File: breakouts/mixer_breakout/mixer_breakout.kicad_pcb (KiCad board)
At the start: 4 copper layers, 24 x 28.5 mm, 131 parts, among them P1 CONN_01X04, U101 CONN_SMA_2GND, U102 CONN_SMA_2GND, U103 CONN_SMA_2GND, U2 LTC5549

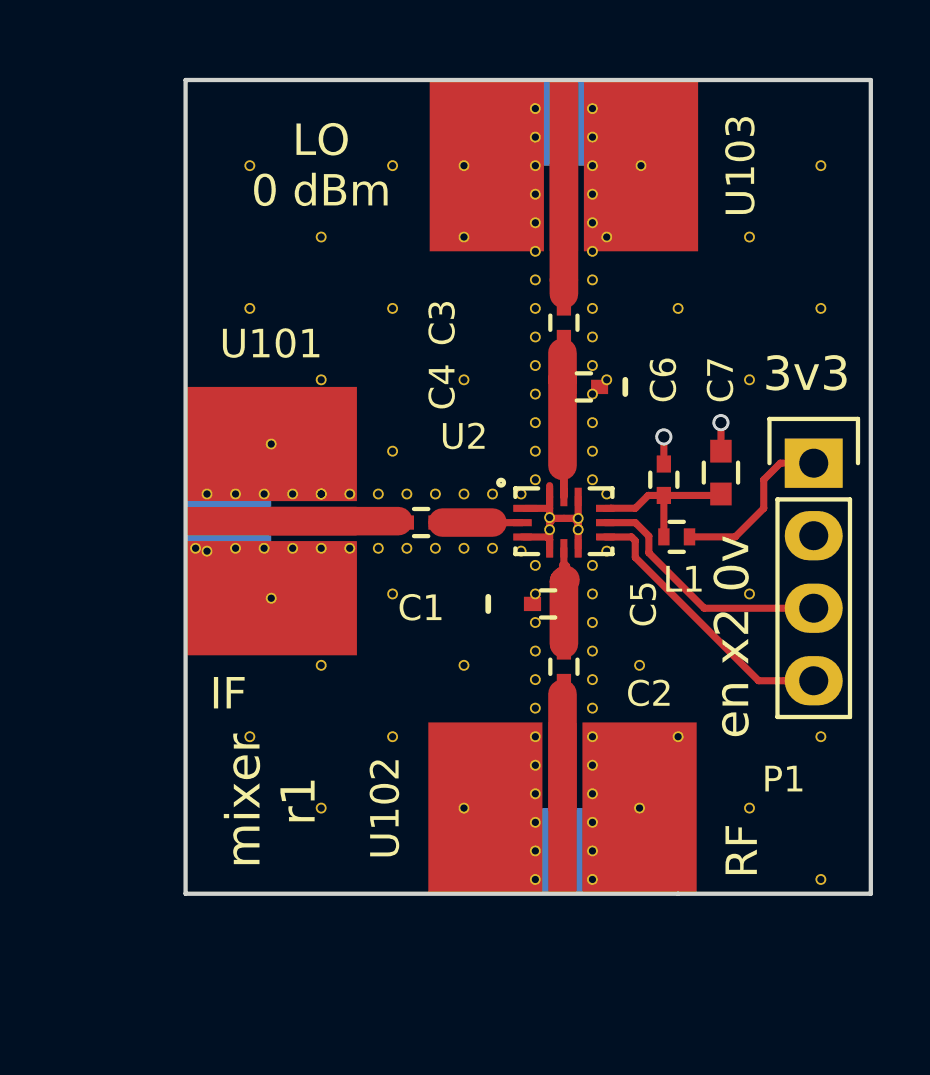
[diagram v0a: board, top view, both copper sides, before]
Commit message: modified mixer breakout to work with ltc5548, moved to soldermask defined pads
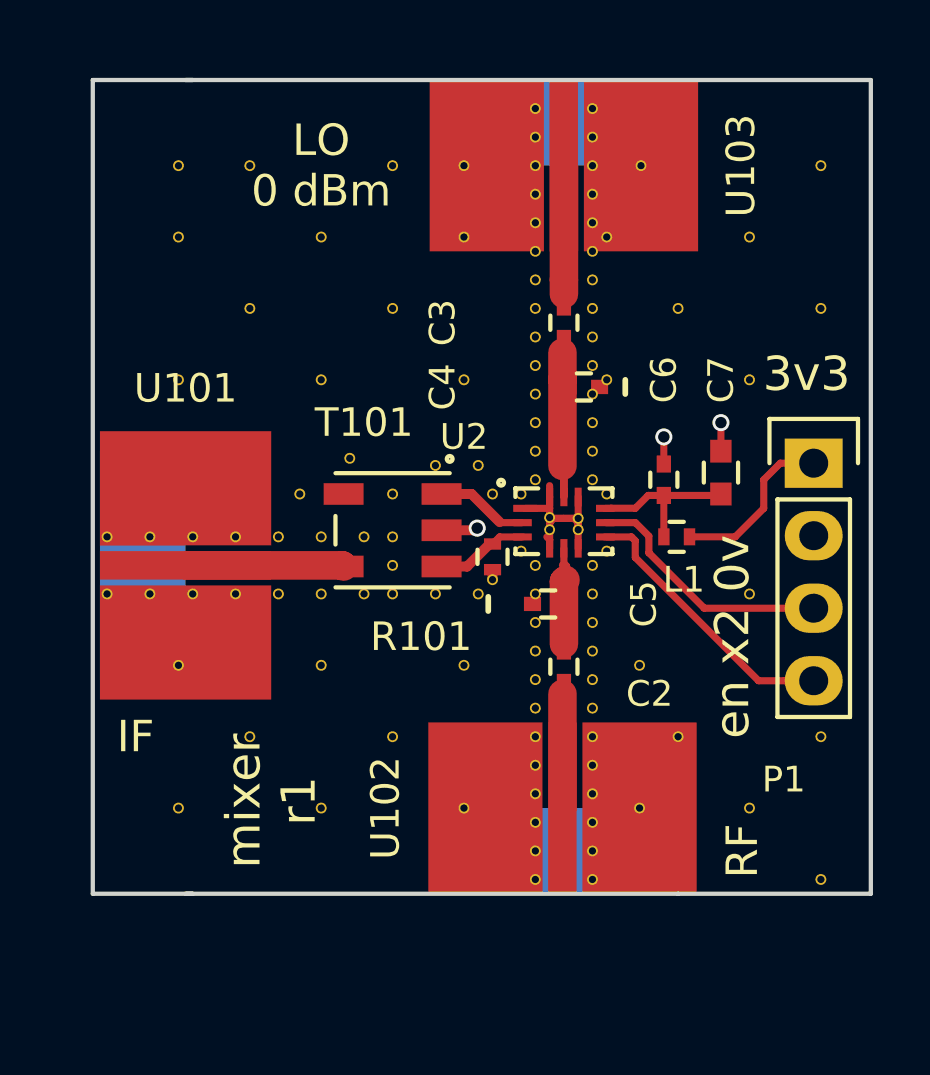
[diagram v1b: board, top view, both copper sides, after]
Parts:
- removed C1: 10 pF, Capacitors_SMD:C_0402
- removed the REF** at (138.2, 107.7)
- removed the REF** at (142.5, 102.5)
- removed the REF** at (142.0, 104.0)
- removed the REF** at (144.0, 104.0)
- removed the REF** at (143.0, 104.0)
- removed the REF** at (145.0, 104.0)
- removed the REF** at (145.0, 105.9)
- removed the REF** at (144.0, 105.9)
- removed the REF** at (143.0, 105.9)
- removed the REF** at (142.0, 105.9)
- removed the REF** at (141.0, 105.9)
- removed the REF** at (140.0, 105.9)
- removed the REF** at (139.0, 105.9)
- removed the REF** at (138.0, 105.9)
- removed the REF** at (137.0, 105.9)
- removed the REF** at (135.6, 105.9)
- removed the REF** at (138.2, 102.2)
- removed the REF** at (136.0, 106.0)
- removed the REF** at (136.0, 104.0)
- removed the REF** at (137.0, 104.0)
- removed the REF** at (138.0, 104.0)
- removed the REF** at (139.0, 104.0)
- added R101: R_Small, Resistors_SMD:R_0402, F.Cu at (146.0, 106.2)
- added REF**: VIA_OSH4LAYER_MIN, vna_footprints:VIA_OSH4LAYER_MIN, F.Cu at (135.0, 92.5)
- added REF**: VIA_OSH4LAYER_MIN, vna_footprints:VIA_OSH4LAYER_MIN, F.Cu at (135.0, 100.0)
- added REF**: VIA_OSH4LAYER_MIN, vna_footprints:VIA_OSH4LAYER_MIN, F.Cu at (135.0, 110.0)
- added REF**: VIA_OSH4LAYER_MIN, vna_footprints:VIA_OSH4LAYER_MIN, F.Cu at (135.0, 115.0)
- added REF**: VIA_OSH4LAYER_MIN, vna_footprints:VIA_OSH4LAYER_MIN, F.Cu at (137.0, 105.5)
- added REF**: VIA_OSH4LAYER_MIN, vna_footprints:VIA_OSH4LAYER_MIN, F.Cu at (134.0, 105.5)
- added REF**: VIA_OSH4LAYER_MIN, vna_footprints:VIA_OSH4LAYER_MIN, F.Cu at (135.5, 105.5)
- added REF**: VIA_OSH4LAYER_MIN, vna_footprints:VIA_OSH4LAYER_MIN, F.Cu at (138.5, 105.5)
- added REF**: VIA_OSH4LAYER_MIN, vna_footprints:VIA_OSH4LAYER_MIN, F.Cu at (140.0, 105.5)
- added REF**: VIA_OSH4LAYER_MIN, vna_footprints:VIA_OSH4LAYER_MIN, F.Cu at (141.5, 105.5)
- added REF**: VIA_OSH4LAYER_MIN, vna_footprints:VIA_OSH4LAYER_MIN, F.Cu at (141.5, 107.5)
- added REF**: VIA_OSH4LAYER_MIN, vna_footprints:VIA_OSH4LAYER_MIN, F.Cu at (142.5, 106.5)
- added REF**: VIA_OSH4LAYER_MIN, vna_footprints:VIA_OSH4LAYER_MIN, F.Cu at (140.0, 107.5)
- added REF**: VIA_OSH4LAYER_MIN, vna_footprints:VIA_OSH4LAYER_MIN, F.Cu at (138.5, 107.5)
- added REF**: VIA_OSH4LAYER_MIN, vna_footprints:VIA_OSH4LAYER_MIN, F.Cu at (137.0, 107.5)
- added REF**: VIA_OSH4LAYER_MIN, vna_footprints:VIA_OSH4LAYER_MIN, F.Cu at (135.5, 107.5)
- added REF**: VIA_OSH4LAYER_MIN, vna_footprints:VIA_OSH4LAYER_MIN, F.Cu at (134.0, 107.5)
- added REF**: VIA_OSH4LAYER_MIN, vna_footprints:VIA_OSH4LAYER_MIN, F.Cu at (132.5, 105.5)
- added REF**: VIA_OSH4LAYER_MIN, vna_footprints:VIA_OSH4LAYER_MIN, F.Cu at (132.5, 107.5)
- added REF**: VIA_OSH4LAYER_MIN, vna_footprints:VIA_OSH4LAYER_MIN, F.Cu at (142.5, 105.5)
- added REF**: VIA_OSH4LAYER_MIN, vna_footprints:VIA_OSH4LAYER_MIN, F.Cu at (145.5, 107.5)
- added REF**: VIA_OSH4LAYER_MIN, vna_footprints:VIA_OSH4LAYER_MIN, F.Cu at (145.5, 103.0)
- added REF**: VIA_OSH4LAYER_MIN, vna_footprints:VIA_OSH4LAYER_MIN, F.Cu at (144.0, 103.0)
- added REF**: VIA_OSH4LAYER_MIN, vna_footprints:VIA_OSH4LAYER_MIN, F.Cu at (144.0, 107.5)
- added REF**: VIA_OSH4LAYER_MIN, vna_footprints:VIA_OSH4LAYER_MIN, F.Cu at (135.0, 95.0)
- added T101: MABAES0060, vna_footprints:5LEAD_BALUN_4p83mm_3p3mm, F.Cu at (142.5, 105.3)
- moved U101 3.38 mm to (135.2, 106.5)
- moved REF** 2.50 mm to (142.5, 104.0)
- moved REF** 1.25 mm to (141.0, 102.8)
- moved REF** 1.10 mm to (146.0, 107.0)
- moved REF** 0.75 mm to (139.2, 104.0)
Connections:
- U2 pad 3: GND -> Net-(R101-Pad1)
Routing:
- net Net-(R101-Pad1): track 0.00 -> 3.64 mm
- net Net-(T101-Pad4): track 4.45 -> 5.55 mm
- net GND: track 9.74 -> 10.5 mm, vias 2 -> 3
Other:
- board size 24 x 28.5 mm -> 27.2 x 28.5 mm
- rule pad_to_mask_clearance: 0.2 -> -0.02

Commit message: finished vna port switch/multiplier board
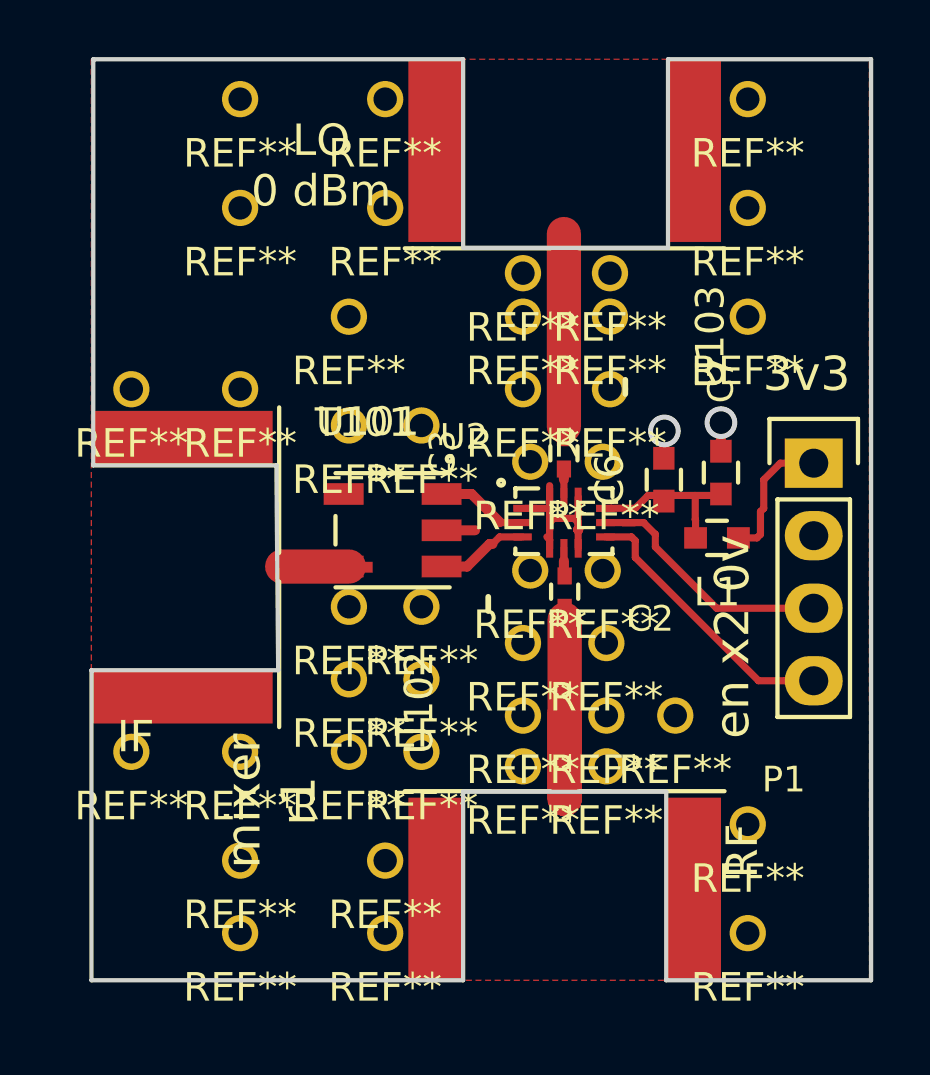
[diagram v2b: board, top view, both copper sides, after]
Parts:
- removed C4, C5: .15 pF, Capacitors_SMD:C_0402
- removed R101: R_Small, Resistors_SMD:R_0402
- removed the REF** at (135.0, 92.5)
- removed the REF** at (135.0, 100.0)
- removed the REF** at (149.5, 95.5)
- removed the REF** at (149.5, 96.5)
- removed the REF** at (149.5, 97.5)
- removed the REF** at (149.5, 98.5)
- removed the REF** at (149.5, 99.5)
- removed the REF** at (149.5, 100.5)
- removed the REF** at (149.5, 101.5)
- removed the REF** at (149.5, 102.5)
- removed the REF** at (149.5, 103.5)
- removed the REF** at (147.0, 106.0)
- removed the REF** at (135.0, 110.0)
- removed the REF** at (150.0, 106.0)
- removed the REF** at (150.0, 104.0)
- removed the REF** at (147.0, 104.0)
- removed the REF** at (149.0, 104.9)
- removed the REF** at (149.0, 105.3)
- removed the REF** at (148.0, 105.3)
- removed the REF** at (148.0, 104.8)
- removed the REF** at (139.2, 104.0)
- removed the REF** at (142.5, 104.0)
- removed the REF** at (141.0, 102.8)
- removed the REF** at (135.0, 115.0)
- removed the REF** at (146.0, 104.0)
- removed the REF** at (146.0, 107.0)
- removed the REF** at (137.0, 105.5)
- removed the REF** at (134.0, 105.5)
- removed the REF** at (135.5, 105.5)
- removed the REF** at (138.5, 105.5)
- removed the REF** at (140.0, 105.5)
- removed the REF** at (141.5, 105.5)
- removed the REF** at (141.5, 107.5)
- removed the REF** at (142.5, 106.5)
- removed the REF** at (140.0, 107.5)
- removed the REF** at (138.5, 107.5)
- removed the REF** at (137.0, 107.5)
- removed the REF** at (135.5, 107.5)
- removed the REF** at (134.0, 107.5)
- removed the REF** at (132.5, 105.5)
- removed the REF** at (132.5, 107.5)
- removed the REF** at (145.0, 92.5)
- removed the REF** at (137.5, 92.5)
- removed the REF** at (142.5, 92.5)
- removed the REF** at (142.5, 105.5)
- removed the REF** at (151.2, 92.5)
- removed the REF** at (157.5, 92.5)
- removed the REF** at (157.5, 117.5)
- removed the REF** at (155.0, 107.5)
- removed the REF** at (137.5, 112.5)
- removed the REF** at (142.5, 112.5)
- removed the REF** at (152.5, 112.5)
- removed the REF** at (157.5, 112.5)
- removed the REF** at (157.5, 97.5)
- removed the REF** at (152.5, 97.5)
- removed the REF** at (145.5, 107.5)
- removed the REF** at (137.5, 97.5)
- removed the REF** at (142.5, 97.5)
- removed the REF** at (145.0, 100.0)
- removed the REF** at (140.0, 100.0)
- removed the REF** at (140.0, 95.0)
- removed the REF** at (145.0, 95.0)
- removed the REF** at (155.0, 95.0)
- removed the REF** at (150.0, 95.0)
- removed the REF** at (150.0, 100.0)
- removed the REF** at (155.0, 100.0)
- removed the REF** at (145.5, 103.0)
- removed the REF** at (155.0, 115.0)
- removed the REF** at (151.2, 110.0)
- removed the REF** at (151.2, 115.0)
- removed the REF** at (145.0, 115.0)
- removed the REF** at (140.0, 115.0)
- removed the REF** at (140.0, 110.0)
- removed the REF** at (145.0, 110.0)
- removed the REF** at (147.5, 106.5)
- removed the REF** at (147.5, 107.5)
- removed the REF** at (147.5, 108.5)
- removed the REF** at (144.0, 103.0)
- removed the REF** at (147.5, 109.5)
- removed the REF** at (147.5, 110.5)
- removed the REF** at (147.5, 111.5)
- removed the REF** at (147.5, 112.5)
- removed the REF** at (147.5, 113.5)
- removed the REF** at (147.5, 114.5)
- removed the REF** at (147.5, 115.5)
- removed the REF** at (147.5, 116.5)
- removed the REF** at (147.5, 117.5)
- removed the REF** at (149.5, 117.5)
- removed the REF** at (144.0, 107.5)
- removed the REF** at (149.5, 116.5)
- removed the REF** at (149.5, 115.5)
- removed the REF** at (149.5, 114.5)
- removed the REF** at (149.5, 113.5)
- removed the REF** at (149.5, 112.5)
- removed the REF** at (149.5, 111.5)
- removed the REF** at (149.5, 110.5)
- removed the REF** at (149.5, 109.5)
- removed the REF** at (149.5, 108.5)
- removed the REF** at (149.5, 107.5)
- removed the REF** at (142.5, 107.5)
- removed the REF** at (149.5, 106.5)
- removed the REF** at (147.5, 103.5)
- removed the REF** at (147.5, 102.5)
- removed the REF** at (147.5, 101.5)
- removed the REF** at (147.5, 100.5)
- removed the REF** at (147.5, 99.5)
- removed the REF** at (147.5, 98.5)
- removed the REF** at (147.5, 97.5)
- removed the REF** at (147.5, 96.5)
- removed the REF** at (147.5, 95.5)
- removed the REF** at (135.0, 95.0)
- removed the REF** at (147.5, 94.5)
- removed the REF** at (147.5, 93.5)
- removed the REF** at (147.5, 92.5)
- removed the REF** at (147.5, 91.5)
- removed the REF** at (147.5, 90.5)
- removed the REF** at (149.5, 90.5)
- removed the REF** at (149.5, 91.5)
- removed the REF** at (149.5, 92.5)
- removed the REF** at (149.5, 93.5)
- removed the REF** at (149.5, 94.5)
- added REF**: DRILL_32p25mil, vna_footprints:DRILL_32p25mil, F.Cu at (147.1, 96.3)
- added REF**: DRILL_32p25mil, vna_footprints:DRILL_32p25mil, F.Cu at (141.0, 113.0)
- added REF**: DRILL_32p25mil, vna_footprints:DRILL_32p25mil, F.Cu at (137.2, 119.4)
- added REF**: DRILL_32p25mil, vna_footprints:DRILL_32p25mil, F.Cu at (137.2, 116.8)
- added REF**: DRILL_32p25mil, vna_footprints:DRILL_32p25mil, F.Cu at (137.2, 90.2)
- added REF**: DRILL_32p25mil, vna_footprints:DRILL_32p25mil, F.Cu at (137.2, 94.0)
- added REF**: DRILL_32p25mil, vna_footprints:DRILL_32p25mil, F.Cu at (141.0, 97.8)
- added REF**: DRILL_32p25mil, vna_footprints:DRILL_32p25mil, F.Cu at (141.0, 101.6)
- added REF**: DRILL_32p25mil, vna_footprints:DRILL_32p25mil, F.Cu at (141.0, 108.0)
- added REF**: DRILL_32p25mil, vna_footprints:DRILL_32p25mil, F.Cu at (147.1, 100.3)
- added REF**: DRILL_32p25mil, vna_footprints:DRILL_32p25mil, F.Cu at (147.1, 97.8)
- added REF**: DRILL_32p25mil, vna_footprints:DRILL_32p25mil, F.Cu at (150.1, 96.3)
- added REF**: DRILL_32p25mil, vna_footprints:DRILL_32p25mil, F.Cu at (150.1, 97.8)
- added REF**: DRILL_32p25mil, vna_footprints:DRILL_32p25mil, F.Cu at (150.1, 100.3)
- added REF**: DRILL_32p25mil, vna_footprints:DRILL_32p25mil, F.Cu at (154.9, 94.0)
- added REF**: DRILL_32p25mil, vna_footprints:DRILL_32p25mil, F.Cu at (154.9, 90.2)
- added REF**: DRILL_32p25mil, vna_footprints:DRILL_32p25mil, F.Cu at (142.2, 90.2)
- added REF**: DRILL_32p25mil, vna_footprints:DRILL_32p25mil, F.Cu at (142.2, 94.0)
- added REF**: DRILL_32p25mil, vna_footprints:DRILL_32p25mil, F.Cu at (137.2, 100.3)
- added REF**: DRILL_32p25mil, vna_footprints:DRILL_32p25mil, F.Cu at (133.3, 100.3)
- added REF**: DRILL_32p25mil, vna_footprints:DRILL_32p25mil, F.Cu at (133.3, 113.0)
- added REF**: DRILL_32p25mil, vna_footprints:DRILL_32p25mil, F.Cu at (137.2, 113.0)
- added REF**: DRILL_32p25mil, vna_footprints:DRILL_32p25mil, F.Cu at (154.9, 97.8)
- added REF**: DRILL_32p25mil, vna_footprints:DRILL_32p25mil, F.Cu at (142.2, 116.8)
- added REF**: DRILL_32p25mil, vna_footprints:DRILL_32p25mil, F.Cu at (142.2, 119.4)
- added REF**: DRILL_32p25mil, vna_footprints:DRILL_32p25mil, F.Cu at (154.9, 119.4)
- added REF**: DRILL_32p25mil, vna_footprints:DRILL_32p25mil, F.Cu at (154.9, 115.6)
- added REF**: DRILL_32p25mil, vna_footprints:DRILL_32p25mil, F.Cu at (152.4, 111.8)
- added REF**: DRILL_32p25mil, vna_footprints:DRILL_32p25mil, F.Cu at (143.5, 101.6)
- added REF**: DRILL_32p25mil, vna_footprints:DRILL_32p25mil, F.Cu at (143.5, 108.0)
- added REF**: DRILL_32p25mil, vna_footprints:DRILL_32p25mil, F.Cu at (147.3, 102.9)
- added REF**: DRILL_32p25mil, vna_footprints:DRILL_32p25mil, F.Cu at (149.9, 102.9)
- added REF**: DRILL_32p25mil, vna_footprints:DRILL_32p25mil, F.Cu at (147.3, 106.7)
- added REF**: DRILL_32p25mil, vna_footprints:DRILL_32p25mil, F.Cu at (147.1, 109.2)
- added REF**: DRILL_32p25mil, vna_footprints:DRILL_32p25mil, F.Cu at (149.9, 106.7)
- added REF**: DRILL_32p25mil, vna_footprints:DRILL_32p25mil, F.Cu at (150.0, 109.2)
- added REF**: DRILL_32p25mil, vna_footprints:DRILL_32p25mil, F.Cu at (150.0, 111.8)
- added REF**: DRILL_32p25mil, vna_footprints:DRILL_32p25mil, F.Cu at (150.0, 113.5)
- added REF**: DRILL_32p25mil, vna_footprints:DRILL_32p25mil, F.Cu at (147.1, 111.8)
- added REF**: DRILL_32p25mil, vna_footprints:DRILL_32p25mil, F.Cu at (147.1, 113.5)
- added REF**: DRILL_32p25mil, vna_footprints:DRILL_32p25mil, F.Cu at (141.0, 110.5)
- added REF**: DRILL_32p25mil, vna_footprints:DRILL_32p25mil, F.Cu at (143.5, 110.5)
- added REF**: DRILL_32p25mil, vna_footprints:DRILL_32p25mil, F.Cu at (143.5, 113.0)
- C6: footprint Capacitors_SMD:C_0402 -> Capacitors_SMD:C_0603
- L1: footprint Resistors_SMD:R_0402 -> Capacitors_SMD:C_0603
- U101, U102, U103: footprint vna_footprints:SMA_CPW_1MM_.2MM -> vna_footprints:142-0721-882_sma_cutout
- moved C3 4.57 mm to (148.5, 102.6)
- moved U102 2.81 mm to (148.5, 117.8), turned to 0 degrees
- moved C2 2.63 mm to (148.5, 107.4)
- moved L1 1.41 mm to (153.9, 105.5)
- moved U103 0.50 mm to (148.5, 92.0), turned to 180 degrees
- moved U101 0.14 mm to (135.1, 106.6), turned to 270 degrees
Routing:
- net Net-(C3-Pad1): track 5.08 -> 14.3 mm
- net Net-(C2-Pad1): track 4.42 -> 12.0 mm
- net Net-(C3-Pad2): track 6.20 -> 0.98 mm
- net Net-(C2-Pad2): track 4.67 -> 0.98 mm
- net Net-(T101-Pad4): track 5.55 -> 2.34 mm
- net VCC: track 6.25 -> 5.03 mm
- net GND: track 10.5 -> 11.0 mm, vias 3 -> 2
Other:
- board size 27.2 x 28.5 mm -> 27.3 x 32.3 mm
- net class Default: clearance 0.127 -> 0.1778
- rule trace_clearance: 0.127 -> 0.1778
- rule trace_min: 0.127 -> 0.2032
